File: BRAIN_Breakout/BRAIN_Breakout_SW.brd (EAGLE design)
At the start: 94.9 x 64.4 mm, 101 parts

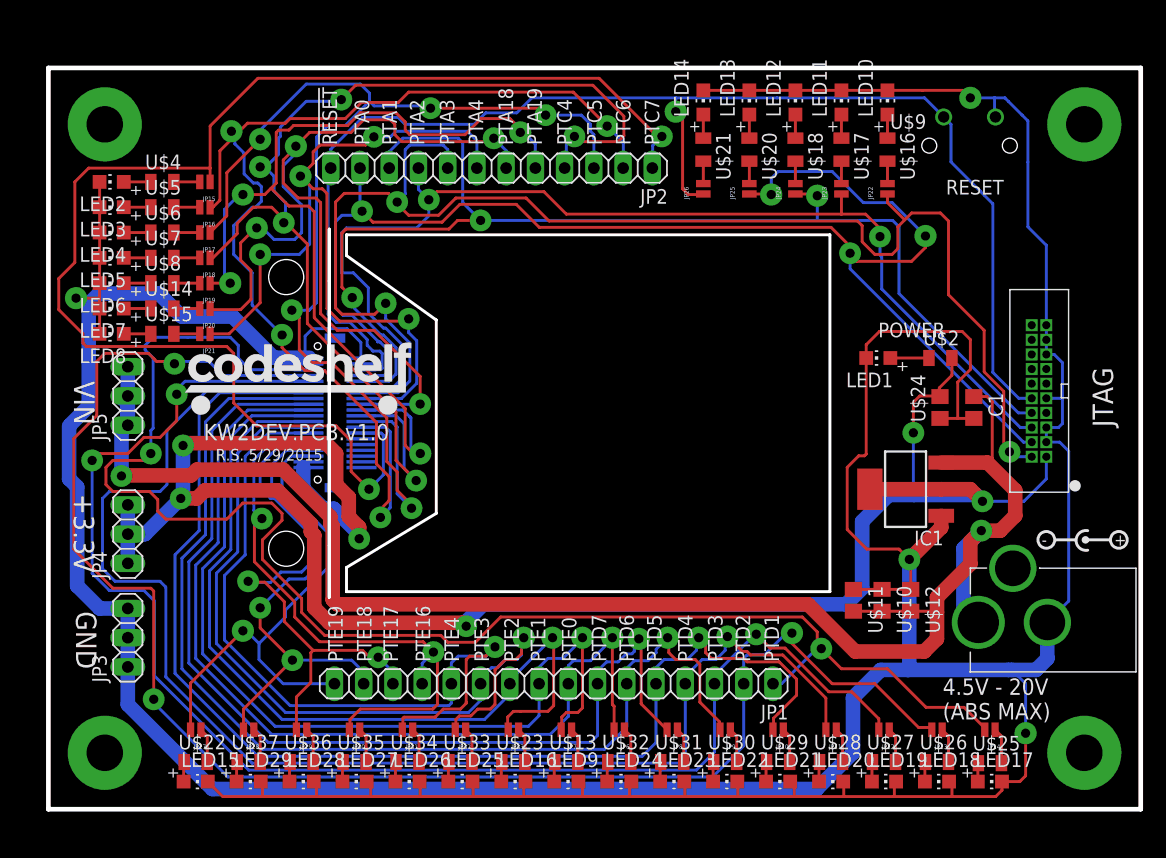
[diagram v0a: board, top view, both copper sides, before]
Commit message: Commit board w/switches & fixes (updated to v1.1)
Hadn't previousy committed produced board (includes Gerbers). Just fixed
JTAG and RESET button ground traces and incremented date + version to
1.1 and 7/16
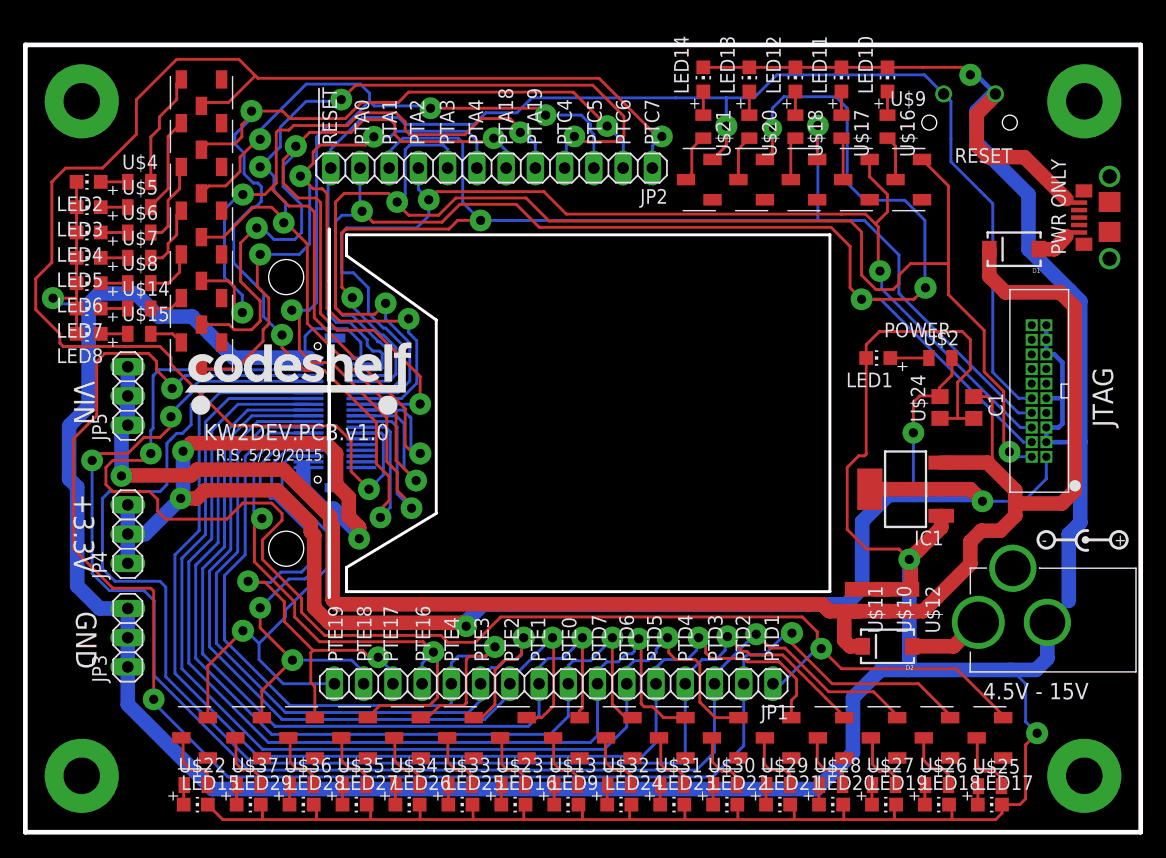
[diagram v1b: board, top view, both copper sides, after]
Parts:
- removed JP10, JP11, JP12, JP13, JP14, JP15, JP16, JP17, JP18, JP19, JP20, JP21, JP22, JP23, JP24, JP25, JP26, JP27, JP28, JP29, JP30, JP31, JP32, JP33, JP6, JP7, JP8, JP9: (no value), SparkFun:SJ_2S-NO-NS
- added D1, D2: (no value), SparkFun:SMA-DIODE
- added U$38, U$39, U$40, U$41, U$42, U$43, U$44, U$45, U$46, U$47, U$48, U$49, U$50, U$51, U$52, U$53, U$54, U$55, U$56, U$57, U$58, U$59, U$60, U$61, U$62, U$63, U$64, U$65: CJS, KW2:CJS
- added X1: USB, SparkFun:USB3076-30-A
- moved LED10 2.00 mm to (108.0, 78.5)
- moved LED11 2.00 mm to (104.0, 78.5)
- moved LED12 2.00 mm to (100.0, 78.5)
- moved LED13 2.00 mm to (96.0, 78.5)
- moved LED14 2.00 mm to (92.0, 78.5)
- moved LED15 2.00 mm to (47.9, 15.5)
- moved LED16 2.00 mm to (75.5, 15.5)
- moved LED17 2.00 mm to (116.9, 15.5)
- moved LED18 2.00 mm to (112.3, 15.5)
- moved LED19 2.00 mm to (107.7, 15.5)
- moved LED2 2.00 mm to (38.6, 69.6)
- moved LED20 2.00 mm to (103.1, 15.5)
- moved LED21 2.00 mm to (98.5, 15.5)
- moved LED22 2.00 mm to (93.9, 15.5)
- moved LED23 2.00 mm to (89.3, 15.5)
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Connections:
- new net N$71: D2.A, U$3.P$1
- new net N$72: D1.A, X1.VCC
- net GND: now also X1.GND
- net N$10: now also U$44.P$1; no longer JP7.1
- net N$11: now also U$65.P$3; no longer JP21.2
- net N$12: now also U$64.P$3; no longer JP20.2
- net N$13: now also U$63.P$3; no longer JP19.2
- net N$14: now also U$62.P$3; no longer JP18.2
- net N$15: now also U$61.P$3; no longer JP17.2
- net N$16: now also U$60.P$3; no longer JP16.2
- net N$17: now also U$59.P$3; no longer JP15.2
- net N$18: now also U$25.2, U$38.P$1; no longer JP6.1, U$32.2
- net N$19: now also U$26.2, U$39.P$1; no longer JP8.1, U$31.2
- net N$20: now also U$27.2, U$40.P$1; no longer JP9.1, U$30.2
- net N$21: now also U$59.P$1; no longer JP15.1
- net N$22: now also U$60.P$1; no longer JP16.1
- net N$23: now also U$61.P$1; no longer JP17.1
- net N$24: now also U$62.P$1; no longer JP18.1
- net N$25: now also U$63.P$1; no longer JP19.1
- net N$26: now also U$64.P$1; no longer JP20.1
- net N$27: now also U$65.P$1; no longer JP21.1
- net N$41: now also U$28.2, U$41.P$1; no longer JP10.1, U$29.2
- net N$42: now also U$29.2, U$42.P$1; no longer JP11.1, U$28.2
- net N$43: now also U$31.2, U$43.P$1; no longer JP14.1, U$25.2
- net N$44: now also U$37.2, U$46.P$1; no longer JP13.1, U$26.2
- net N$45: now also U$36.2, U$47.P$1; no longer JP12.1, U$27.2
- net N$48: now also U$54.P$3; no longer JP22.1
- net N$50: now also U$54.P$1; no longer JP22.2
- net N$51: now also U$55.P$3; no longer JP23.1
- net N$53: now also U$55.P$1; no longer JP23.2
- net N$54: now also U$56.P$3; no longer JP24.1
- net N$56: now also U$56.P$1; no longer JP24.2
- net N$57: now also U$57.P$3; no longer JP25.1
- net N$59: now also U$57.P$1; no longer JP25.2
- net N$60: now also U$58.P$3; no longer JP26.1
- net N$62: now also U$58.P$1; no longer JP26.2
- net N$64: now also U$45.P$1; no longer JP27.1
- net N$65: now also U$35.2, U$48.P$1; no longer JP28.1, U$37.2
- net N$66: now also U$34.2, U$49.P$1; no longer JP29.1, U$36.2
- net N$67: now also U$33.2, U$50.P$1; no longer JP30.1, U$35.2
- net N$68: now also U$23.2, U$51.P$1; no longer JP31.1, U$34.2
- net N$69: now also U$32.2, U$52.P$1; no longer JP32.1, U$33.2
- net N$70: now also U$30.2, U$53.P$1; no longer JP33.1, U$23.2
- net PTD1: now also U$38.P$3; no longer JP14.2
- net PTD2: now also U$39.P$3; no longer JP13.2
- net PTD3: now also U$40.P$3; no longer JP12.2
- net PTD4: now also U$41.P$3; no longer JP11.2
- net PTD5: now also U$42.P$3; no longer JP10.2
- net PTD6: now also U$53.P$3; no longer JP9.2
- net PTD7: now also U$43.P$3; no longer JP8.2
- net PTE0: now also U$52.P$3; no longer JP6.2
- net PTE1: now also U$44.P$3; no longer JP7.2
- net PTE16: now also U$48.P$3; no longer JP30.2
- net PTE17: now also U$47.P$3; no longer JP29.2
- net PTE18: now also U$46.P$3; no longer JP28.2
- net PTE19: now also U$45.P$3; no longer JP27.2
- net PTE2: now also U$51.P$3; no longer JP33.2
- net PTE3: now also U$50.P$3; no longer JP32.2
- net PTE4: now also U$49.P$3; no longer JP31.2
- net V+: now also D1.C, D2.C; no longer U$3.P$1
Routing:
- net GND: track 430.0 -> 464.7 mm
- net V+: track 143.2 -> 158.4 mm, vias 2 -> 1
- net N$57: track 121.4 -> 133.5 mm
- net N$17: track 2.25 -> 10.00 mm
- net N$21: track 120.1 -> 127.5 mm
- net N$25: track 84.4 -> 91.2 mm
- net N$71: track 0.00 -> 6.60 mm
- net N$16: track 2.25 -> 8.40 mm
- net N$54: track 108.2 -> 113.9 mm
- net N$15: track 2.25 -> 7.35 mm
- net N$27: track 72.6 -> 77.6 mm
- net N$51: track 98.0 -> 102.9 mm
- net N$48: track 124.9 -> 129.5 mm
- net PTD1: track 132.4 -> 128.0 mm
- net N$72: track 0.00 -> 4.15 mm
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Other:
- board size 94.9 x 64.4 mm -> 96.9 x 68.4 mm
- board text added: "4.5V - 15V"
- board text added: "PWR ONLY"
- board text removed: "4.5V - 20V (ABS MAX)"
